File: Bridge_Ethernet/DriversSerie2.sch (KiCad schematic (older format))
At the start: 12 parts, among them U3 MAX3222CDW, U4 ISL83485

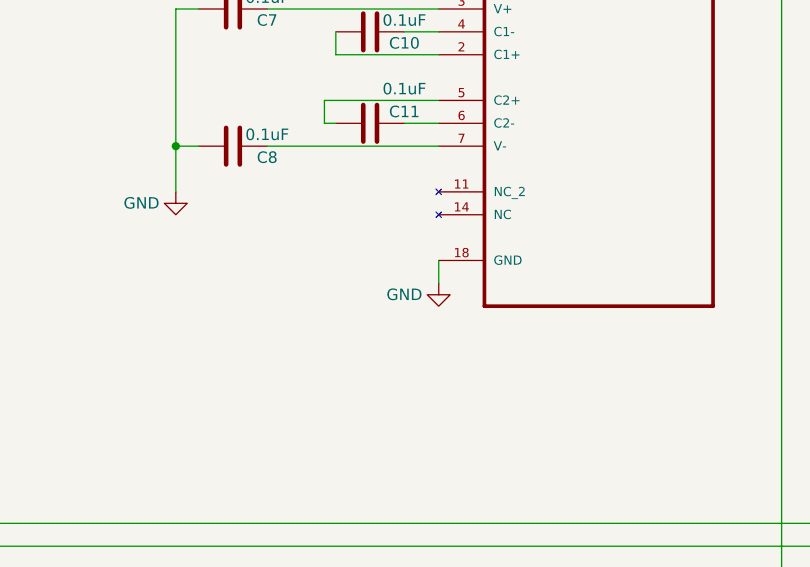
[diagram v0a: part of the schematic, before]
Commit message: Esquemático Finalizado, sin warnings. Haciendo asignaciones de footprints
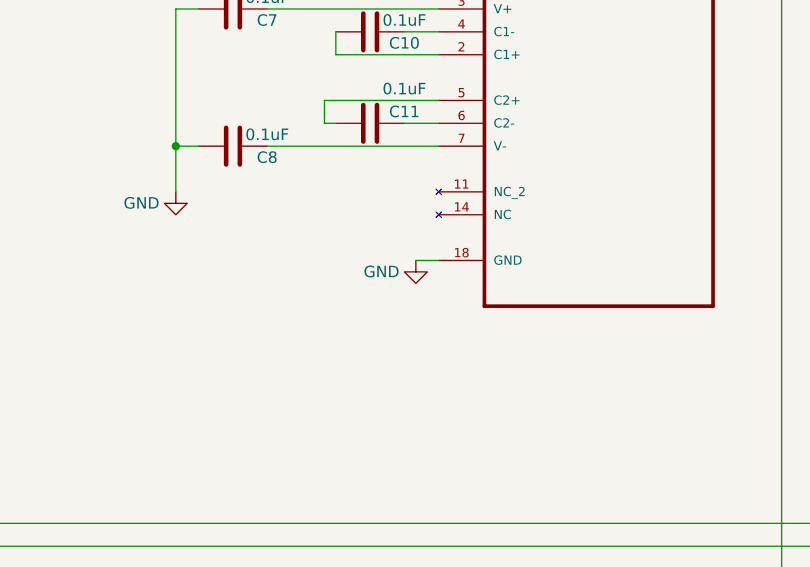
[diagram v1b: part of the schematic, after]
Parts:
- U3: footprint SOIC127P1032X265-20N -> MAX3222CDW:SOIC127P1032X265-20N
- U4: footprint (none) -> SOIC127P600X175-8N:SOIC127P600X175-8N
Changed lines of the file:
@@
 F 0 "U3" H 4200 4170 50  0000 C CNN
 F 1 "MAX3222CDW" H 4200 4079 50  0000 C CNN
-F 2 "SOIC127P1032X265-20N" H 4200 2800 50  0001 L BNN
+F 2 "MAX3222CDW:SOIC127P1032X265-20N" H 4200 2800 50  0001 L BNN
 F 3 "Unavailable" H 4200 2800 50  0001 L BNN
 F 4 "3-V to 5.5-V Multichannel S-232 Line Driver/ eceiver 20-SOIC 0 to 70" H 4200 2800 50  0001 L BNN "Field4"
@@
 L power:GND #PWR017
 U 1 1 5D8C2762
-P 3500 4100
-F 0 "#PWR017" H 3500 3850 50  0001 C CNN
-F 1 "GND" H 3350 4050 50  0000 C CNN
-F 2 "" H 3500 4100 50  0001 C CNN
-F 3 "" H 3500 4100 50  0001 C CNN
-	1    3500 4100
-	1    0    0    -1
-$EndComp
-Wire Wire Line
-	3500 4000 3500 4100
+P 3400 4000
+F 0 "#PWR017" H 3400 3750 50  0001 C CNN
+F 1 "GND" H 3250 3950 50  0000 C CNN
+F 2 "" H 3400 4000 50  0001 C CNN
+F 3 "" H 3400 4000 50  0001 C CNN
+	1    3400 4000
+	1    0    0    -1
+$EndComp
 Wire Wire Line
 	4900 2100 5000 2100
@@
 F 0 "U4" H 5900 5850 50  0000 C CNN
 F 1 "ISL83485" H 6000 5750 50  0000 C CNN
-F 2 "" H 5900 6650 50  0001 C CNN
+F 2 "SOIC127P600X175-8N:SOIC127P600X175-8N" H 5900 6650 50  0001 C CNN
 F 3 "" H 5900 6650 50  0001 C CNN
 	1    5200 5750
@@
 Text HLabel 8050 3100 0    50   Input ~ 0
 RX_232_2
+Wire Wire Line
+	3500 4000 3400 4000
 $EndSCHEMATC

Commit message: Esquemático Finalizado. Asignaciones Realizadas. Comienzo de PCB.
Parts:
- C10, C11, C12, C7, C8, C9: footprint (none) -> Capacitor_SMD:C_0805_2012Metric
- D6, D7: footprint (none) -> Diode_SMD:D_SMB_Modified
- R3, R4: footprint (none) -> Resistor_SMD:R_0805_2012Metric
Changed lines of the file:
@@
 F 0 "C9" H 3115 1346 50  0000 L CNN
 F 1 "0.1uF" H 3115 1255 50  0000 L CNN
-F 2 "" H 3038 1150 50  0001 C CNN
+F 2 "Capacitor_SMD:C_0805_2012Metric" H 3038 1150 50  0001 C CNN
 F 3 "~" H 3000 1300 50  0001 C CNN
 	1    3000 1300
@@
 F 0 "C10" V 3250 3150 50  0000 C CNN
 F 1 "0.1uF" V 3150 3150 50  0000 C CNN
-F 2 "" H 3238 2850 50  0001 C CNN
+F 2 "Capacitor_SMD:C_0805_2012Metric" H 3238 2850 50  0001 C CNN
 F 3 "~" H 3200 3000 50  0001 C CNN
 	1    3200 3000
@@
 F 0 "C11" V 3150 3550 50  0000 C CNN
 F 1 "0.1uF" V 3050 3550 50  0000 C CNN
-F 2 "" H 3238 3250 50  0001 C CNN
+F 2 "Capacitor_SMD:C_0805_2012Metric" H 3238 3250 50  0001 C CNN
 F 3 "~" H 3200 3400 50  0001 C CNN
 	1    3200 3400
@@
 F 0 "C12" H 5965 4346 50  0000 L CNN
 F 1 "0.1uF" H 5965 4255 50  0000 L CNN
-F 2 "" H 5888 4150 50  0001 C CNN
+F 2 "Capacitor_SMD:C_0805_2012Metric" H 5888 4150 50  0001 C CNN
 F 3 "~" H 5850 4300 50  0001 C CNN
 	1    5850 4300
@@
 F 0 "R3" H 6620 4946 50  0000 L CNN
 F 1 "4K7" H 6620 4855 50  0000 L CNN
-F 2 "" V 6480 4900 50  0001 C CNN
+F 2 "Resistor_SMD:R_0805_2012Metric" V 6480 4900 50  0001 C CNN
 F 3 "~" H 6550 4900 50  0001 C CNN
 	1    6550 4900
@@
 F 0 "R4" H 6620 5746 50  0000 L CNN
 F 1 "4K7" H 6620 5655 50  0000 L CNN
-F 2 "" V 6480 5700 50  0001 C CNN
+F 2 "Resistor_SMD:R_0805_2012Metric" V 6480 5700 50  0001 C CNN
 F 3 "~" H 6550 5700 50  0001 C CNN
 	1    6550 5700
@@
 F 0 "C8" V 2650 3650 50  0000 C CNN
 F 1 "0.1uF" V 2550 3650 50  0000 C CNN
-F 2 "" H 2638 3350 50  0001 C CNN
+F 2 "Capacitor_SMD:C_0805_2012Metric" H 2638 3350 50  0001 C CNN
 F 3 "~" H 2600 3500 50  0001 C CNN
 	1    2600 3500
@@
 F 0 "C7" V 2650 3050 50  0000 C CNN
 F 1 "0.1uF" V 2550 3050 50  0000 C CNN
-F 2 "" H 2638 2750 50  0001 C CNN
+F 2 "Capacitor_SMD:C_0805_2012Metric" H 2638 2750 50  0001 C CNN
 F 3 "~" H 2600 2900 50  0001 C CNN
 	1    2600 2900
@@
 F 0 "D6" H 8425 2775 50  0000 C CNN
 F 1 "GL05T-E3-08" H 8425 2684 50  0000 C CNN
-F 2 "" H 8550 2300 50  0001 C CNN
+F 2 "Diode_SMD:D_SMB_Modified" H 8550 2300 50  0001 C CNN
 F 3 "" H 8550 2300 50  0001 C CNN
 	1    8500 2250
@@
 F 0 "D7" H 8425 3925 50  0000 C CNN
 F 1 "GL05T-E3-08" H 8425 3834 50  0000 C CNN
-F 2 "" H 8550 3450 50  0001 C CNN
+F 2 "Diode_SMD:D_SMB_Modified" H 8550 3450 50  0001 C CNN
 F 3 "" H 8550 3450 50  0001 C CNN
 	1    8500 3400

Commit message: Esquemático Finalizado. Asignaciones Realizadas. Componentes acomodados en PCB.
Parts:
- renumbered D6 to D3, D7 to D4
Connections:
- net GNDREF is gone; now on net GND: D3.2, D4.2
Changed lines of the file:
@@
 $EndComp
 $Comp
-L Device:C C9
-U 1 1 5D8BBC3A
-P 3000 1300
-F 0 "C9" H 3115 1346 50  0000 L CNN
-F 1 "0.1uF" H 3115 1255 50  0000 L CNN
-F 2 "Capacitor_SMD:C_0805_2012Metric" H 3038 1150 50  0001 C CNN
-F 3 "~" H 3000 1300 50  0001 C CNN
-	1    3000 1300
-	1    0    0    -1
-$EndComp
-$Comp
-L power:GND #PWR015
+L power:GND #PWR013
 U 1 1 5D8BC83D
 P 3000 1550
-F 0 "#PWR015" H 3000 1300 50  0001 C CNN
+F 0 "#PWR013" H 3000 1300 50  0001 C CNN
 F 1 "GND" H 3150 1500 50  0000 C CNN
 F 2 "" H 3000 1550 50  0001 C CNN
@@
 	3000 1450 3000 1550
 $Comp
-L power:+3V3 #PWR014
+L power:+3V3 #PWR012
 U 1 1 5DE5D7A1
 P 3000 900
-F 0 "#PWR014" H 3000 750 50  0001 C CNN
+F 0 "#PWR012" H 3000 750 50  0001 C CNN
 F 1 "+3V3" H 3015 1073 50  0000 C CNN
 F 2 "" H 3000 900 50  0001 C CNN
@@
 	3000 1050 3000 1150
 $Comp
-L power:GND #PWR016
+L power:GND #PWR014
 U 1 1 5DE5D7AB
 P 3400 2150
-F 0 "#PWR016" H 3400 1900 50  0001 C CNN
+F 0 "#PWR014" H 3400 1900 50  0001 C CNN
 F 1 "GND" H 3250 2100 50  0000 C CNN
 F 2 "" H 3400 2150 50  0001 C CNN
@@
 NoConn ~ 4900 2200
 $Comp
-L power:GND #PWR017
+L power:GND #PWR015
 U 1 1 5D8C2762
 P 3400 4000
-F 0 "#PWR017" H 3400 3750 50  0001 C CNN
+F 0 "#PWR015" H 3400 3750 50  0001 C CNN
 F 1 "GND" H 3250 3950 50  0000 C CNN
 F 2 "" H 3400 4000 50  0001 C CNN
@@
 	5850 4450 5850 4550
 $Comp
-L power:+3V3 #PWR019
+L power:+3V3 #PWR017
 U 1 1 5DE5D7C8
 P 5850 3900
-F 0 "#PWR019" H 5850 3750 50  0001 C CNN
+F 0 "#PWR017" H 5850 3750 50  0001 C CNN
 F 1 "+3V3" H 5865 4073 50  0000 C CNN
 F 2 "" H 5850 3900 50  0001 C CNN
@@
 $EndComp
 $Comp
-L power:GND #PWR020
+L power:GND #PWR018
 U 1 1 5DE5D7C5
 P 5850 4550
-F 0 "#PWR020" H 5850 4300 50  0001 C CNN
+F 0 "#PWR018" H 5850 4300 50  0001 C CNN
 F 1 "GND" H 6000 4500 50  0000 C CNN
 F 2 "" H 5850 4550 50  0001 C CNN
@@
 	5850 4100 5850 4150
 $Comp
-L power:GND #PWR018
+L power:GND #PWR016
 U 1 1 5D8E35E2
 P 5700 6050
-F 0 "#PWR018" H 5700 5800 50  0001 C CNN
+F 0 "#PWR016" H 5700 5800 50  0001 C CNN
 F 1 "GND" H 5550 6000 50  0000 C CNN
 F 2 "" H 5700 6050 50  0001 C CNN
@@
 	1300 2300 3500 2300
 $Comp
-L power:GND #PWR013
+L power:GND #PWR011
 U 1 1 5DE5D7BD
 P 2350 3700
-F 0 "#PWR013" H 2350 3450 50  0001 C CNN
+F 0 "#PWR011" H 2350 3450 50  0001 C CNN
 F 1 "GND" H 2200 3650 50  0000 C CNN
 F 2 "" H 2350 3700 50  0001 C CNN
@@
 AR Path="/5DA0E4A1/5DC83719" Ref="D?"  Part="1"
 AR Path="/5DA0E587/5DC83719" Ref="D?"  Part="1"
-AR Path="/5DA10068/5DC83719" Ref="D6"  Part="1"
-AR Path="/5DC83719" Ref="D6"  Part="1"
-F 0 "D6" H 8425 2775 50  0000 C CNN
+AR Path="/5DA10068/5DC83719" Ref="D3"  Part="1"
+AR Path="/5DC83719" Ref="D?"  Part="1"
+F 0 "D3" H 8425 2775 50  0000 C CNN
 F 1 "GL05T-E3-08" H 8425 2684 50  0000 C CNN
 F 2 "Diode_SMD:D_SMB_Modified" H 8550 2300 50  0001 C CNN
@@
 AR Path="/5DA0E4A1/5DC8371F" Ref="D?"  Part="1"
 AR Path="/5DA0E587/5DC8371F" Ref="D?"  Part="1"
-AR Path="/5DA10068/5DC8371F" Ref="D7"  Part="1"
-AR Path="/5DC8371F" Ref="D7"  Part="1"
-F 0 "D7" H 8425 3925 50  0000 C CNN
+AR Path="/5DA10068/5DC8371F" Ref="D4"  Part="1"
+AR Path="/5DC8371F" Ref="D?"  Part="1"
+F 0 "D4" H 8425 3925 50  0000 C CNN
 F 1 "GL05T-E3-08" H 8425 3834 50  0000 C CNN
 F 2 "Diode_SMD:D_SMB_Modified" H 8550 3450 50  0001 C CNN
@@
 	1    0    0    -1
 $EndComp
-$Comp
-L power:GNDREF #PWR?
-U 1 1 5DC83725
-P 8250 2250
-AR Path="/5D9FFB34/5DC83725" Ref="#PWR?"  Part="1"
-AR Path="/5DA0E4A1/5DC83725" Ref="#PWR?"  Part="1"
-AR Path="/5DA0E587/5DC83725" Ref="#PWR?"  Part="1"
-AR Path="/5DA10068/5DC83725" Ref="#PWR011"  Part="1"
-F 0 "#PWR011" H 8250 2000 50  0001 C CNN
-F 1 "GNDREF" H 8255 2077 50  0001 C CNN
-F 2 "" H 8250 2250 50  0001 C CNN
-F 3 "" H 8250 2250 50  0001 C CNN
-	1    8250 2250
-	1    0    0    -1
-$EndComp
 Wire Wire Line
 	8250 2250 8250 2150
-$Comp
-L power:GNDREF #PWR?
-U 1 1 5DC8372C
-P 8250 3400
-AR Path="/5D9FFB34/5DC8372C" Ref="#PWR?"  Part="1"
-AR Path="/5DA0E4A1/5DC8372C" Ref="#PWR?"  Part="1"
-AR Path="/5DA0E587/5DC8372C" Ref="#PWR?"  Part="1"
-AR Path="/5DA10068/5DC8372C" Ref="#PWR012"  Part="1"
-F 0 "#PWR012" H 8250 3150 50  0001 C CNN
-F 1 "GNDREF" H 8255 3227 50  0001 C CNN
-F 2 "" H 8250 3400 50  0001 C CNN
-F 3 "" H 8250 3400 50  0001 C CNN
-	1    8250 3400
-	1    0    0    -1
-$EndComp
 Wire Wire Line
 	8250 3400 8250 3300
@@
 Wire Wire Line
 	3500 4000 3400 4000
+$Comp
+L power:GND #PWR?
+U 1 1 5DC9DB30
+P 8250 3400
+AR Path="/5D9FFB34/5DC9DB30" Ref="#PWR?"  Part="1"
+AR Path="/5DA10068/5DC9DB30" Ref="#PWR020"  Part="1"
+F 0 "#PWR020" H 8250 3150 50  0001 C CNN
+F 1 "GND" H 8255 3227 50  0000 C CNN
+F 2 "" H 8250 3400 50  0001 C CNN
+F 3 "" H 8250 3400 50  0001 C CNN
+	1    8250 3400
+	1    0    0    -1
+$EndComp
+$Comp
+L power:GND #PWR?
+U 1 1 5DCA0922
+P 8250 2250
+AR Path="/5D9FFB34/5DCA0922" Ref="#PWR?"  Part="1"
+AR Path="/5DA10068/5DCA0922" Ref="#PWR019"  Part="1"
+F 0 "#PWR019" H 8250 2000 50  0001 C CNN
+F 1 "GND" H 8255 2077 50  0000 C CNN
+F 2 "" H 8250 2250 50  0001 C CNN
+F 3 "" H 8250 2250 50  0001 C CNN
+	1    8250 2250
+	1    0    0    -1
+$EndComp
+$Comp
+L Device:C C9
+U 1 1 5D8BBC3A
+P 3000 1300
+F 0 "C9" H 3115 1346 50  0000 L CNN
+F 1 "0.1uF" H 3115 1255 50  0000 L CNN
+F 2 "Capacitor_SMD:C_0805_2012Metric" H 3038 1150 50  0001 C CNN
+F 3 "~" H 3000 1300 50  0001 C CNN
+	1    3000 1300
+	1    0    0    -1
+$EndComp
 $EndSCHEMATC

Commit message: Esquemático Finalizado. Asignaciones Realizadas. Reacomodamiento de componentes. Inicio de Ruteo.
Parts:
- D3, D4: footprint Diode_SMD:D_SMB_Modified -> SOT95P280X125-3N:SOT95P280X125-3N
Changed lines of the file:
@@
 F 0 "D3" H 8425 2775 50  0000 C CNN
 F 1 "GL05T-E3-08" H 8425 2684 50  0000 C CNN
-F 2 "Diode_SMD:D_SMB_Modified" H 8550 2300 50  0001 C CNN
+F 2 "SOT95P280X125-3N:SOT95P280X125-3N" H 8550 2300 50  0001 C CNN
 F 3 "" H 8550 2300 50  0001 C CNN
 	1    8500 2250
@@
 F 0 "D4" H 8425 3925 50  0000 C CNN
 F 1 "GL05T-E3-08" H 8425 3834 50  0000 C CNN
-F 2 "Diode_SMD:D_SMB_Modified" H 8550 3450 50  0001 C CNN
+F 2 "SOT95P280X125-3N:SOT95P280X125-3N" H 8550 3450 50  0001 C CNN
 F 3 "" H 8550 3450 50  0001 C CNN
 	1    8500 3400
